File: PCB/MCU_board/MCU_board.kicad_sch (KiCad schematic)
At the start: 13 parts, among them IC3 ESP32-S3-WROOM-1-N4R8, J1 DS1013-40SSIB1-B-0

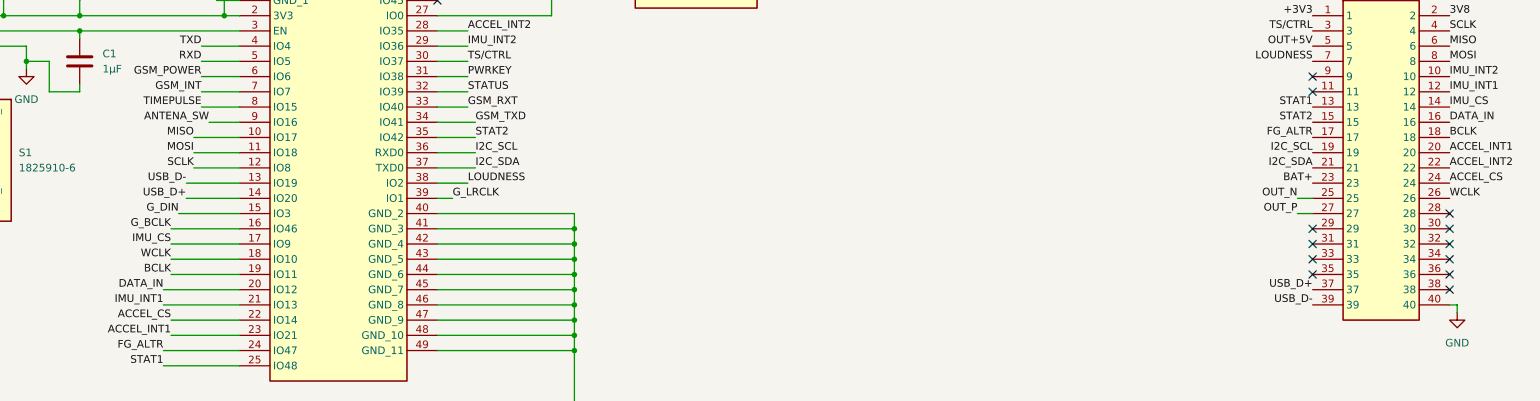
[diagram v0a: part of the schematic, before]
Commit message: ATA connector updated
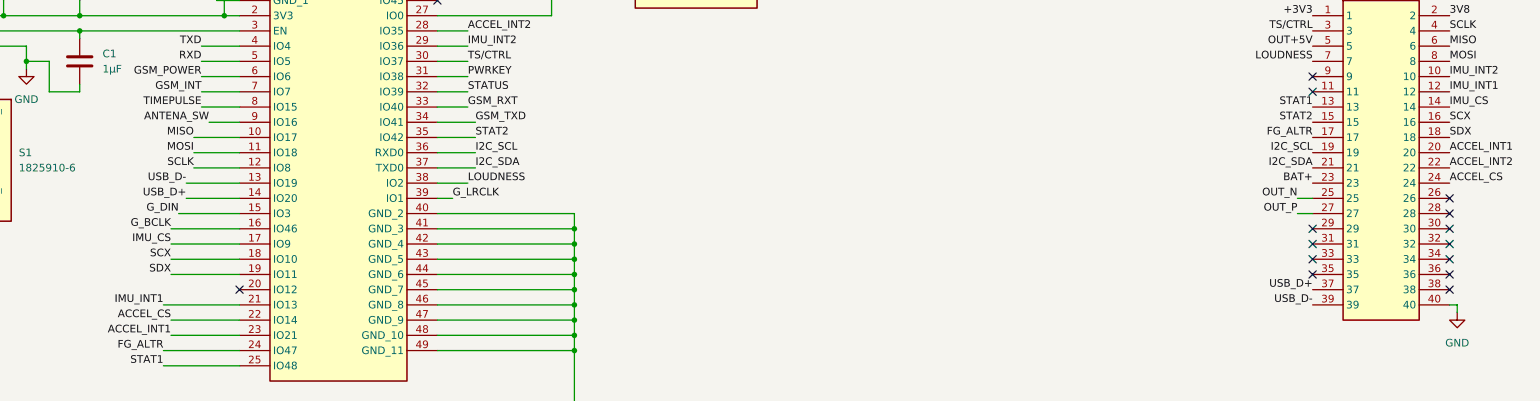
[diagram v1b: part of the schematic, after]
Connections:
- net BCLK renamed SDX
- net DATA_IN: no longer names the net of IC3.20 (IO12)
- net DATA_IN: no longer J1.16
- net WCLK: no longer names the net of J1.26
- net WCLK: no longer IC3.18 (IO10)
- new net SCX: IC3.18 (IO10), J1.16
- no-connect marks 17 -> 19
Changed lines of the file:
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@@
+	)
+	(no_connect
+		(at 274.32 68.58)
 	)
 	(no_connect
@@
 	)
 	(no_connect
+		(at 72.39 83.82)
+	)
+	(no_connect
 		(at 274.32 81.28)
 	)
@@
 	(wire
 		(pts
-			(xy 59.69 83.82) (xy 72.39 83.82)
-		)
-		(stroke
-			(width 0)
-			(type default)
-		)
-	)
-	(wire
-		(pts
 			(xy 29.21 40.64) (xy 45.72 40.64)
 		)
@@
 		)
 	)
-	(label "DATA_IN"
-		(at 274.32 55.88 0)
-		(effects
-			(font
-				(size 1.27 1.27)
-			)
-			(justify left bottom)
-		)
-	)
 	(label "TXD"
 		(at 152.4 167.64 90)
@@
 		)
 	)
+	(label "SDX"
+		(at 274.32 58.42 0)
+		(effects
+			(font
+				(size 1.27 1.27)
+			)
+			(justify left bottom)
+		)
+	)
 	(label "OUT_P"
 		(at 101.6 166.37 90)
@@
 		)
 	)
-	(label "BCLK"
-		(at 274.32 58.42 0)
-		(effects
-			(font
-				(size 1.27 1.27)
-			)
-			(justify left bottom)
-		)
-	)
 	(label "SCLK"
 		(at 64.77 63.5 180)
@@
 		)
 	)
-	(label "BCLK"
-		(at 60.96 81.28 180)
-		(effects
-			(font
-				(size 1.27 1.27)
-			)
-			(justify right bottom)
-		)
-	)
 	(label "IMU_INT1"
 		(at 274.32 50.8 0)
@@
 		)
 	)
-	(label "WCLK"
-		(at 274.32 68.58 0)
+	(label "SCX"
+		(at 274.32 55.88 0)
 		(effects
 			(font
@@
 		)
 	)
-	(label "WCLK"
-		(at 60.96 78.74 180)
-		(effects
-			(font
-				(size 1.27 1.27)
-			)
-			(justify right bottom)
-		)
-	)
 	(label "RXD"
 		(at 149.86 167.64 90)
@@
 		)
 	)
-	(label "DATA_IN"
-		(at 59.69 83.82 180)
-		(effects
-			(font
-				(size 1.27 1.27)
-			)
-			(justify right bottom)
-		)
-	)
 	(label "ACCEL_CS"
 		(at 274.32 66.04 0)
@@
 		)
 	)
+	(label "SCX"
+		(at 60.96 78.74 180)
+		(effects
+			(font
+				(size 1.27 1.27)
+			)
+			(justify right bottom)
+		)
+	)
+	(label "SDX"
+		(at 60.96 81.28 180)
+		(effects
+			(font
+				(size 1.27 1.27)
+			)
+			(justify right bottom)
+		)
+	)

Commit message: modified gnd
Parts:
- C1, C3: footprint Capacitor_THT:C_Disc_D5.0mm_W2.5mm_P2.50mm -> Capacitor_SMD:CP_Elec_6.3x5.4
- C4: footprint Capacitor_THT:CP_Radial_Tantal_D5.0mm_P2.50mm -> Capacitor_Tantalum_SMD:CP_EIA-3216-18_Kemet-A
- R29, R30: footprint Resistor_THT:R_Axial_DIN0207_L6.3mm_D2.5mm_P7.62mm_Horizontal -> Resistor_SMD:R_0603_1608Metric
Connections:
- net 3V8 is gone; now on net BAT+: J1.2
- net BAT+: no longer J1.23
- no-connect marks 19 -> 20
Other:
- sheet Stationary ports: added none; removed 3V8
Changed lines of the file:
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@@
 	)
 	(no_connect
+		(at 251.46 66.04)
+	)
+	(no_connect
 		(at 274.32 71.12)
 	)
@@
 	(wire
 		(pts
-			(xy 168.91 182.88) (xy 165.1 182.88)
-		)
-		(stroke
-			(width 0)
-			(type default)
-		)
-	)
-	(wire
-		(pts
 			(xy 132.08 167.64) (xy 132.08 171.45)
 		)
@@
 		)
 	)
-	(label "3V8"
-		(at 274.32 38.1 0)
-		(effects
-			(font
-				(size 1.27 1.27)
-			)
-			(justify left bottom)
-		)
-	)
 	(label "G_LRCLK"
 		(at 107.95 68.58 0)
@@
 		)
 	)
-	(label "3V8"
-		(at 168.91 182.88 0)
-		(effects
-			(font
-				(size 1.27 1.27)
-			)
-			(justify left bottom)
-		)
-	)
 	(label "PWRKEY"
 		(at 110.49 48.26 0)
@@
 		)
 	)
-	(label "BAT+"
-		(at 251.46 66.04 180)
-		(effects
-			(font
-				(size 1.27 1.27)
-			)
-			(justify right bottom)
-		)
-	)
 	(label "LOUDNESS"
 		(at 140.97 167.64 90)
@@
 		)
 	)
+	(global_label "BAT+"
+		(shape input)
+		(at 274.32 38.1 0)
+		(fields_autoplaced yes)
+		(effects
+			(font
+				(size 1.27 1.27)
+			)
+			(justify left)
+		)
+		(property "Intersheetrefs" "${INTERSHEET_REFS}"
+			(at 282.2038 38.1 0)
+			(hide yes)
+			(show_name no)
+			(do_not_autoplace no)
+			(effects
+				(font
+					(size 1.27 1.27)
+				)
+				(justify left)
+			)
+		)
+	)
 	(symbol
 		(lib_id "Device:R")
@@
 			)
 		)
-		(property "Footprint" "Resistor_THT:R_Axial_DIN0207_L6.3mm_D2.5mm_P7.62mm_Horizontal"
+		(property "Footprint" "Resistor_SMD:R_0603_1608Metric"
 			(at 22.86 38.862 90)
 			(hide yes)
@@
 			)
 		)
-		(property "Footprint" "Capacitor_THT:C_Disc_D5.0mm_W2.5mm_P2.50mm"
+		(property "Footprint" "Capacitor_SMD:CP_Elec_6.3x5.4"
 			(at 33.9852 35.56 0)
 			(hide yes)
@@
 			)
 		)
-		(property "Footprint" "Capacitor_THT:CP_Radial_Tantal_D5.0mm_P2.50mm"
+		(property "Footprint" "Capacitor_Tantalum_SMD:CP_EIA-3216-18_Kemet-A"
 			(at 46.6852 35.56 0)
 			(hide yes)
@@
 			)
 		)
-		(property "Footprint" "Capacitor_THT:C_Disc_D5.0mm_W2.5mm_P2.50mm"
+		(property "Footprint" "Capacitor_SMD:CP_Elec_6.3x5.4"
 			(at 46.6852 49.53 0)
 			(hide yes)
@@
 			)
 		)
-		(property "Footprint" "Resistor_THT:R_Axial_DIN0207_L6.3mm_D2.5mm_P7.62mm_Horizontal"
+		(property "Footprint" "Resistor_SMD:R_0603_1608Metric"
 			(at 126.238 27.94 90)
 			(hide yes)
@@
 			)
 		)
-		(pin "OUTP" output
+		(pin "OUTP" input
 			(at 101.6 171.45 90)
 			(effects
@@
 			)
 		)
-		(pin "OUT_N" output
+		(pin "OUT_N" input
 			(at 104.14 171.45 90)
 			(effects
 				(font
-					(size 1.27 1.27)
-				)
-				(justify right)
-			)
-		)
-		(pin "3V8" output
-			(at 165.1 182.88 0)
-			(effects
-				(font
